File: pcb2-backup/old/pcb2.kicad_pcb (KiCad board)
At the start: 2 copper layers, 100 x 102.4 mm, 72 parts, among them J1 WQP419GR_audio_in_1, J10 ACJS-HHOP_pedal_3, J11 ACJS-HHOP_pedal_4, J12 PMOD_JD, J13 PMOD_JC, J14 ACJS-HHOP_audio_out_L, J15 ACJS-HHOP_audio_out_R, J2 WQP419GR_audio_in_3, J3 Barrel_+5V_in, J4 Conn_+5V_to_FPGA, J5 Conn_GND_to_FPGA, J6 WQP419GR_audio_in_2, J7 WQP419GR_audio_in_4, J8 ACJS-HHOP_pedal_1, J9 ACJS-HHOP_pedal_2, U1 LM3940, U2 PCM1840, U3 ADC104S021, U4 TAD5242

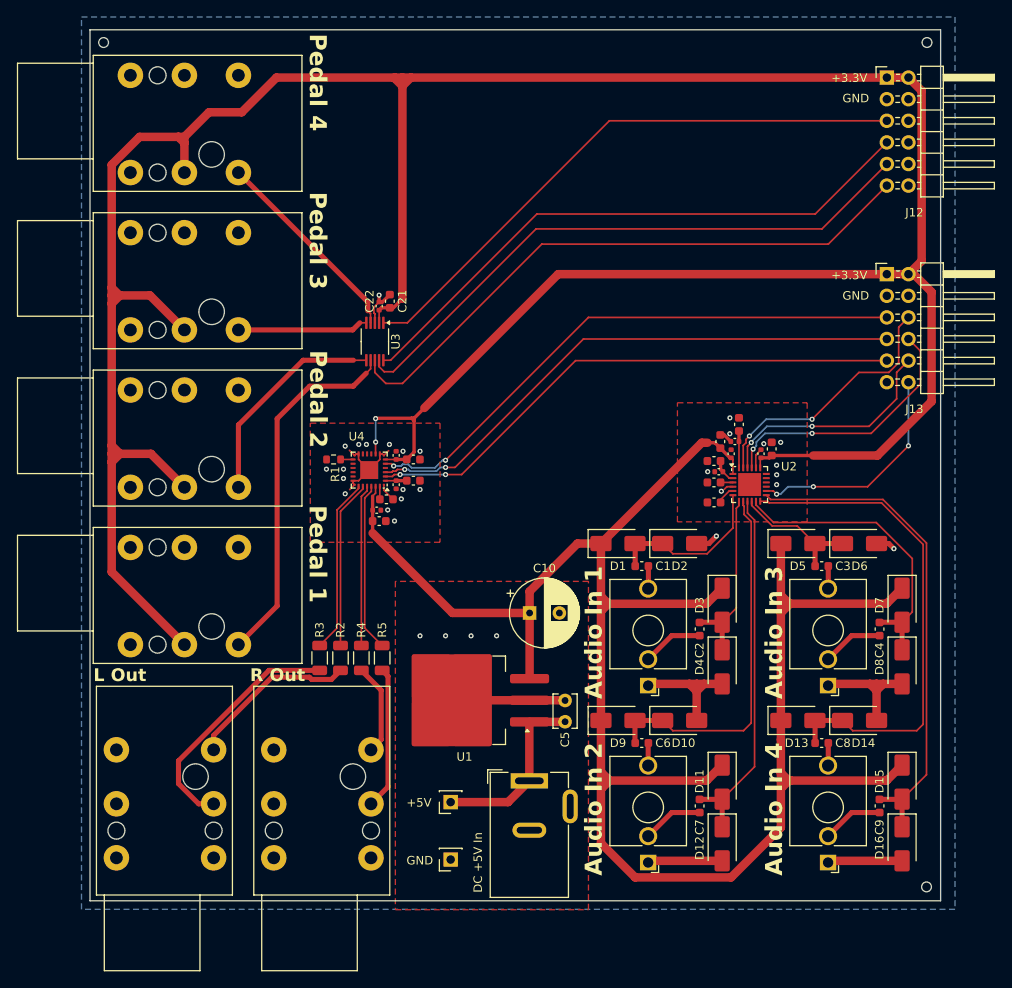
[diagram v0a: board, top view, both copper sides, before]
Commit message: Implement expression pedal controls
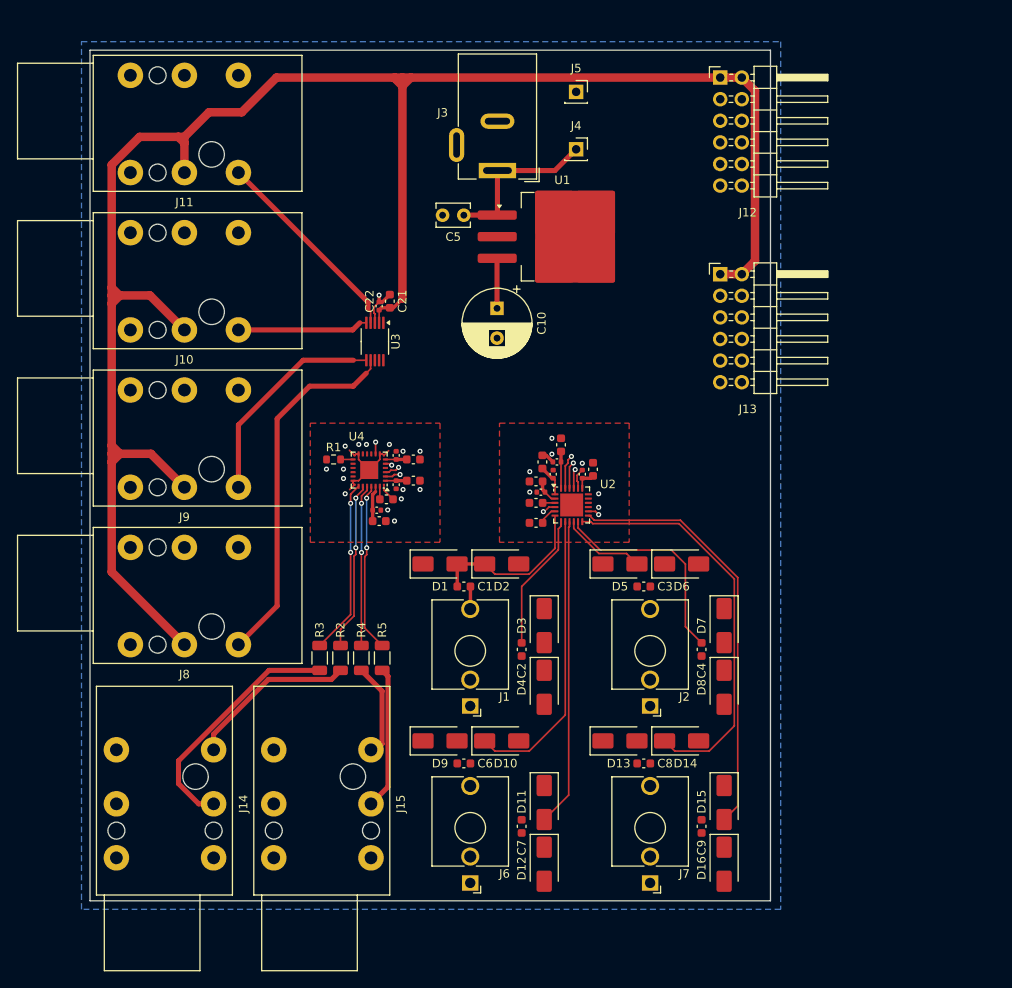
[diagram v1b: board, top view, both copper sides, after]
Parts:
- removed ToolingHole_JLCPCB_BR, ToolingHole_JLCPCB_TL, ToolingHole_JLCPCB_TR: ToolingHole_JLCPCB, 0_MountingHole:ToolingHole_JLCPCB
- moved J5 91.4 mm to (163.8, 41.0), turned to 0 degrees
- moved J4 78.2 mm to (163.8, 47.8), turned to 0 degrees
- moved J3 71.8 mm to (154.5, 50.3), turned to 180 degrees
- moved C5 60.7 mm to (150.6, 55.5), turned to 180 degrees
- moved U1 55.7 mm to (162.1, 58.1), turned to 0 degrees
- moved C10 36.0 mm to (154.4, 66.5), turned to -90 degrees
- moved C17 21.1 mm to (165.7, 85.4)
- moved C18 21.1 mm to (164.5, 86.0)
- moved C13 21.1 mm to (159.0, 91.7)
- moved C15 21.1 mm to (159.6, 88.1)
- moved C2 21.1 mm to (157.3, 106.6)
- moved C3 21.1 mm to (171.7, 99.2)
- moved C7 21.1 mm to (157.3, 127.4)
- moved C8 21.1 mm to (171.7, 120.0)
- moved J2 21.1 mm to (172.4, 113.2)
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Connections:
- J12 pad 11: /ADC_PEDAL_DIN -> /DAC_DIN
- J12 pad 5: /ADC_PEDAL_CS -> unconnected-(J12-Pin_5-Pad5)
- J12 pad 7: /ADC_PEDAL_CLK -> /DAC_FSYNC
- J12 pad 9: /ADC_PEDAL_DOUT -> /DAC_CLK
- J13 pad 10: /ADC_AUDIO_CLK -> /ADC_AUDIO_DOUT
- J13 pad 11: unconnected-(J13-Pin_11-Pad11) -> /ADC_PEDAL_CS
- J13 pad 5: /DAC_DIN -> /ADC_PEDAL_CLK
- J13 pad 7: /DAC_FSYNC -> /ADC_PEDAL_DOUT
- J13 pad 8: /ADC_AUDIO_DOUT -> /ADC_AUDIO_CLK
- J13 pad 9: /DAC_CLK -> /ADC_PEDAL_DIN
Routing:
- net +3.3VA: track 237.4 -> 13.9 mm
- net +3.3V: track 369.3 -> 236.3 mm, vias 2 -> 1
- net /ADC_PEDAL_DIN: track 71.8 -> 0.00 mm
- net /ADC_PEDAL_DOUT: track 70.8 -> 0.00 mm
- net /ADC_PEDAL_CLK: track 69.8 -> 0.00 mm
- net /ADC_PEDAL_CS: track 69.0 -> 0.00 mm
- net GND: track 90.5 -> 23.8 mm, vias 31 -> 24
- net /DAC_DIN: track 66.6 -> 0.81 mm, vias 2 -> 1
- net /DAC_FSYNC: track 65.6 -> 1.79 mm, vias 2 -> 1
- net /DAC_CLK: track 64.6 -> 1.82 mm, vias 2 -> 1
- net /ADC_AUDIO_DOUT: track 31.2 -> 2.27 mm, vias 2 -> 1
- net /ADC_AUDIO_FSYNC: track 31.0 -> 4.04 mm, vias 2 -> 1
- net /ADC_AUDIO_SHDNZ: track 26.7 -> 1.37 mm, vias 3 -> 1
- net /ADC_AUDIO_CLK: track 27.5 -> 3.16 mm, vias 2 -> 1
- net /ADC_IN4P: track 58.6 -> 47.9 mm
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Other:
- board size 100 x 102.4 mm -> 80 x 100 mm
- board text removed: "+3.3V"
- board text removed: "+5V"
- board text removed: "Audio In 1"
- board text removed: "Audio In 2"
- board text removed: "Audio In 3"
- board text removed: "Audio In 4"
- board text removed: "DC +5V In"
- board text removed: "GND"
- board text removed: "L Out"
- board text removed: "Pedal 1"
- board text removed: "Pedal 2"
- board text removed: "Pedal 3"
- board text removed: "Pedal 4"
- board text removed: "R Out"
